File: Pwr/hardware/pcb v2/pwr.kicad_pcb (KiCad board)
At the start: 4 copper layers, 82.8 x 110 mm, 59 parts, among them J1 XT60, J10 Conn_ARM_JTAG_SWD_10, J11 Conn_01x06, J12 Conn_01x06, J13 Conn_01x06, J14 Conn_01x06, J15 XT60, J2 FFC2B35-10-T, J3 114020164, J4 XT60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

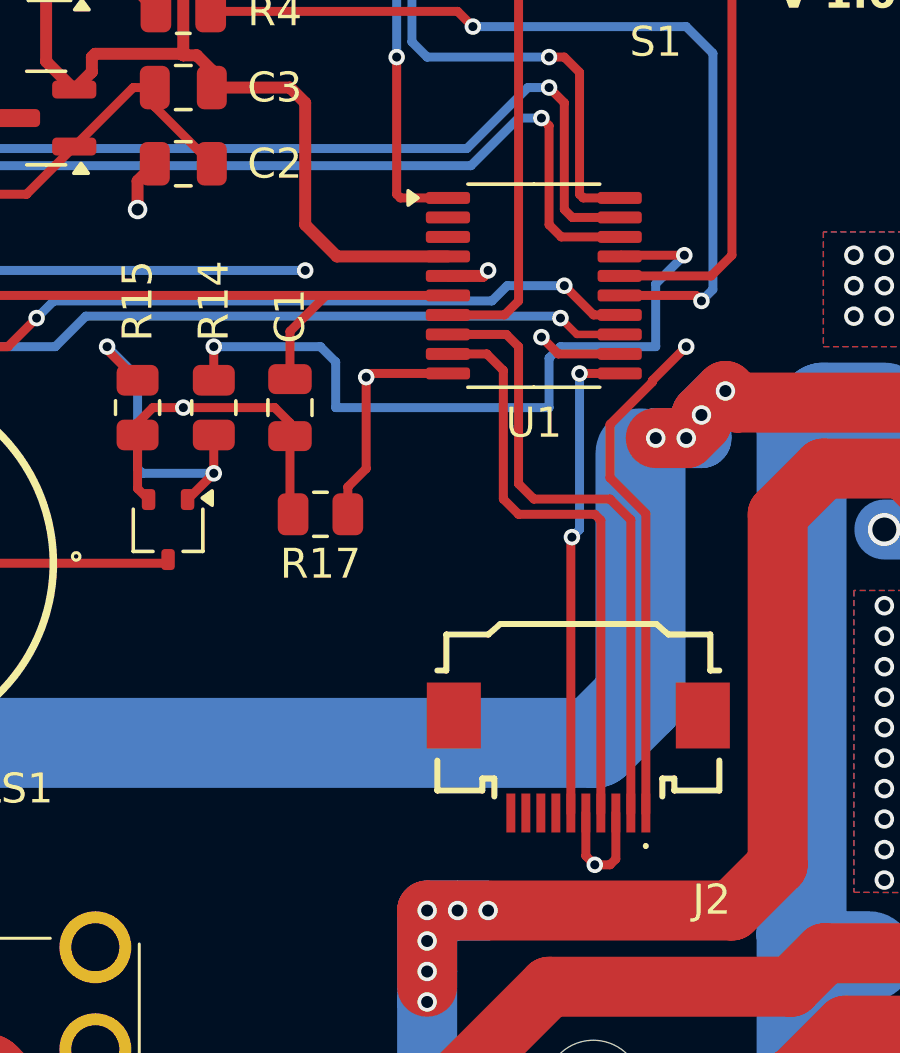
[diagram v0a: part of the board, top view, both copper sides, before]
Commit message: Correction sur l'ecran SPI
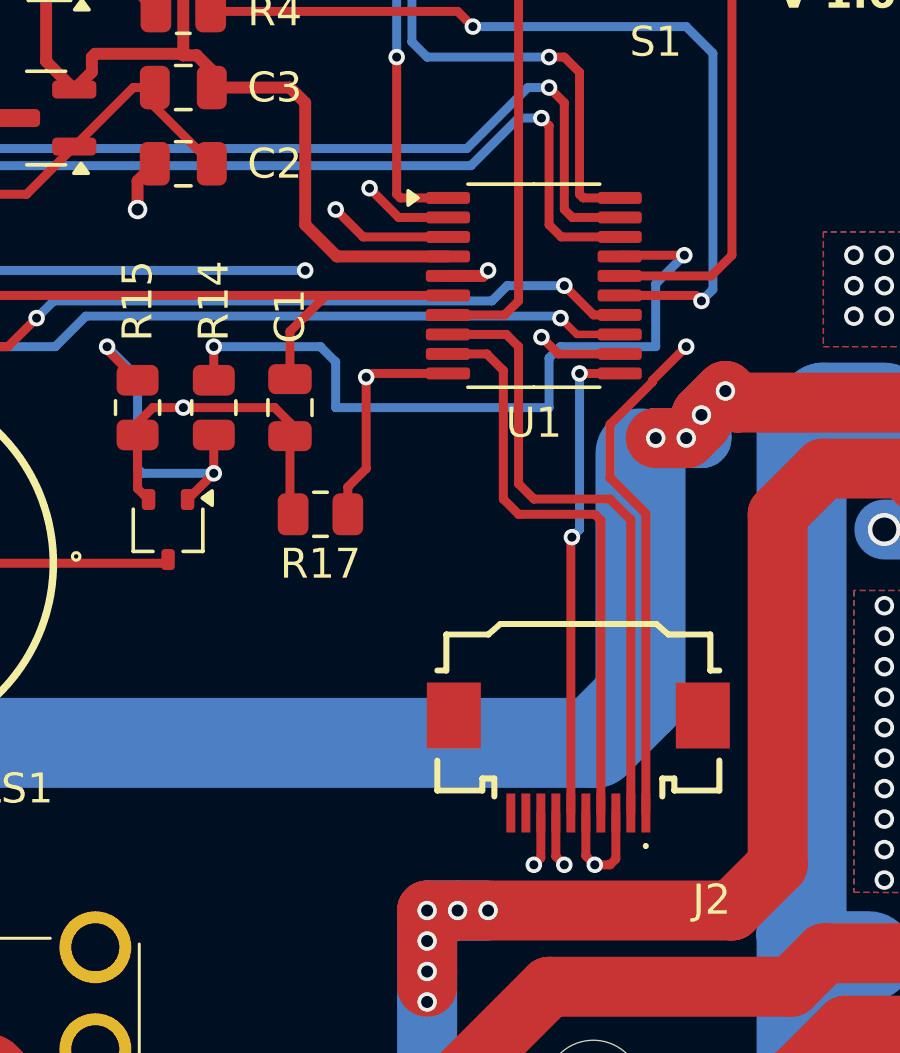
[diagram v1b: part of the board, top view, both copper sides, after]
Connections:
- J2 pad 7: unconnected-(J2-Pad7) -> /CPU - Debug/DISPLAY_RESET
- J2 pad 8: unconnected-(J2-Pad8) -> /CPU - Debug/DISPLAY_CD
- U1 pad 2: unconnected-(U1-PC14-Pad2) -> /CPU - Debug/DISPLAY_CD
- U1 pad 3: unconnected-(U1-PC15-Pad3) -> /CPU - Debug/DISPLAY_RESET
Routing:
- net /CPU - Debug/DISPLAY_CD: track 0.00 -> 41.1 mm, vias 0 -> 2
- net /CPU - Debug/DISPLAY_RESET: track 0.00 -> 37.6 mm, vias 0 -> 2
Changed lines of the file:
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@@
 	(net 56 "unconnected-(RV2-Pad1)")
 	(net 57 "unconnected-(RV3-Pad3)")
-	(net 58 "unconnected-(J2-Pad8)")
+	(net 58 "/CPU - Debug/DISPLAY_CD")
 	(net 59 "Net-(Q4-D)")
 	(net 60 "Net-(Q4-G)")
@@
 	(net 65 "Net-(Q6-G)")
 	(net 66 "/CPU - Debug/BUZZER")
-	(net 67 "unconnected-(U1-PC14-Pad2)")
-	(net 68 "unconnected-(U1-PC15-Pad3)")
-	(net 69 "unconnected-(J2-Pad7)")
-	(net 70 "Net-(R5-Pad2)")
-	(net 71 "Net-(J10-GNDDetect)")
+	(net 67 "/CPU - Debug/DISPLAY_RESET")
+	(net 68 "Net-(R5-Pad2)")
+	(net 69 "Net-(J10-GNDDetect)")
 	(footprint "Capacitor_SMD:C_0805_2012Metric"
 		(layer "F.Cu")
@@
 			(layers "F.Cu" "F.Paste" "F.Mask")
 			(roundrect_rratio 0.25)
-			(net 67 "unconnected-(U1-PC14-Pad2)")
+			(net 58 "/CPU - Debug/DISPLAY_CD")
 			(pinfunction "PC14")
-			(pintype "bidirectional+no_connect")
+			(pintype "bidirectional")
 		)
 		(pad "3" smd roundrect
@@
 			(layers "F.Cu" "F.Paste" "F.Mask")
 			(roundrect_rratio 0.25)
-			(net 68 "unconnected-(U1-PC15-Pad3)")
+			(net 67 "/CPU - Debug/DISPLAY_RESET")
 			(pinfunction "PC15")
-			(pintype "bidirectional+no_connect")
+			(pintype "bidirectional")
 		)
 		(pad "4" smd roundrect
@@
 			(size 0.74 2.79)
 			(layers "F.Cu" "F.Paste" "F.Mask")
-			(net 71 "Net-(J10-GNDDetect)")
+			(net 69 "Net-(J10-GNDDetect)")
 			(pinfunction "GNDDetect")
 			(pintype "passive")
@@
 			)
 			(remove_unused_layers no)
-			(net 70 "Net-(R5-Pad2)")
+			(net 68 "Net-(R5-Pad2)")
 			(pinfunction "6")
 			(pintype "passive")
@@
 			(layers "F.Cu" "F.Paste" "F.Mask")
 			(roundrect_rratio 0.243902)
-			(net 71 "Net-(J10-GNDDetect)")
+			(net 69 "Net-(J10-GNDDetect)")
 			(pintype "passive")
 		)
@@
 			(size 0.3 1.3)
 			(layers "F.Cu" "F.Paste" "F.Mask")
-			(net 69 "unconnected-(J2-Pad7)")
+			(net 67 "/CPU - Debug/DISPLAY_RESET")
 			(pinfunction "7")
-			(pintype "passive+no_connect")
+			(pintype "passive")
 		)
 		(pad "8" smd rect
@@
 			(size 0.3 1.3)
 			(layers "F.Cu" "F.Paste" "F.Mask")
-			(net 58 "unconnected-(J2-Pad8)")
+			(net 58 "/CPU - Debug/DISPLAY_CD")
 			(pinfunction "8")
-			(pintype "passive+no_connect")
+			(pintype "passive")
 		)
 		(pad "9" smd rect
@@
 			(layers "F.Cu" "F.Paste" "F.Mask")
 			(roundrect_rratio 0.243902)
-			(net 70 "Net-(R5-Pad2)")
+			(net 68 "Net-(R5-Pad2)")
 			(pintype "passive")
 		)
@@
 	)
 	(segment
+		(start 160.1 62.503106)
+		(end 160.1 62.5)
+		(width 0.3)
+		(layer "F.Cu")
+		(net 58)
+	)
+	(segment
+		(start 165.81 84.818)
+		(end 165.81 83.325)
+		(width 0.3)
+		(layer "F.Cu")
+		(net 58)
+	)
+	(segment
+		(start 162.7135 63.473)
+		(end 161.069894 63.473)
+		(width 0.3)
+		(layer "F.Cu")
+		(net 58)
+	)
+	(segment
+		(start 161.069894 63.473)
+		(end 160.1 62.503106)
+		(width 0.3)
+		(layer "F.Cu")
+		(net 58)
+	)
+	(segment
+		(start 165.576 85.052)
+		(end 165.81 84.818)
+		(width 0.3)
+		(layer "F.Cu")
+		(net 58)
+	)
+	(via
+		(at 160.1 62.5)
+		(size 0.55)
+		(drill 0.3)
+		(layers "F.Cu" "B.Cu")
+		(net 58)
+	)
+	(via
+		(at 165.576 85.052)
+		(size 0.55)
+		(drill 0.3)
+		(layers "F.Cu" "B.Cu")
+		(net 58)
+	)
+	(segment
+		(start 168.965 69.135)
+		(end 168.624 69.476)
+		(width 0.3)
+		(layer "In1.Cu")
+		(net 58)
+	)
+	(segment
+		(start 168.6 62.5)
+		(end 169.1 63)
+		(width 0.3)
+		(layer "In1.Cu")
+		(net 58)
+	)
+	(segment
+		(start 160.1 62.5)
+		(end 168.6 62.5)
+		(width 0.3)
+		(layer "In1.Cu")
+		(net 58)
+	)
+	(segment
+		(start 168.624 69.476)
+		(end 168.624 86.068)
+		(width 0.3)
+		(layer "In1.Cu")
+		(net 58)
+	)
+	(segment
+		(start 165.576 85.56)
+		(end 165.576 85.052)
+		(width 0.3)
+		(layer "In1.Cu")
+		(net 58)
+	)
+	(segment
+		(start 168.965 63.135)
+		(end 168.965 69.135)
+		(width 0.3)
+		(layer "In1.Cu")
+		(net 58)
+	)
+	(segment
+		(start 169.1 63)
+		(end 168.965 63.135)
+		(width 0.3)
+		(layer "In1.Cu")
+		(net 58)
+	)
+	(segment
+		(start 168.624 86.068)
+		(end 166.084 86.068)
+		(width 0.3)
+		(layer "In1.Cu")
+		(net 58)
+	)
+	(segment
+		(start 166.084 86.068)
+		(end 165.576 85.56)
+		(width 0.3)
+		(layer "In1.Cu")
+		(net 58)
+	)
+	(segment
 		(start 128.492 73.368)
 		(end 129 72.86)
@@
 	)
 	(segment
+		(start 166.592 85.052)
+		(end 166.31 84.77)
+		(width 0.3)
+		(layer "F.Cu")
+		(net 67)
+	)
+	(segment
+		(start 162.7135 64.123)
+		(end 159.887 64.123)
+		(width 0.3)
+		(layer "F.Cu")
+		(net 67)
+	)
+	(segment
+		(start 166.31 84.77)
+		(end 166.31 83.325)
+		(width 0.3)
+		(layer "F.Cu")
+		(net 67)
+	)
+	(segment
+		(start 159.887 64.123)
+		(end 158.972 63.208)
+		(width 0.3)
+		(layer "F.Cu")
+		(net 67)
+	)
+	(via
+		(at 158.972 63.208)
+		(size 0.55)
+		(drill 0.3)
+		(layers "F.Cu" "B.Cu")
+		(net 67)
+	)
+	(via
+		(at 166.592 85.052)
+		(size 0.55)
+		(drill 0.3)
+		(layers "F.Cu" "B.Cu")
+		(net 67)
+	)
+	(segment
+		(start 168.116 63.208)
+		(end 168.116 83.528)
+		(width 0.3)
+		(layer "In1.Cu")
+		(net 67)
+	)
+	(segment
+		(start 158.972 63.208)
+		(end 168.116 63.208)
+		(width 0.3)
+		(layer "In1.Cu")
+		(net 67)
+	)
+	(segment
+		(start 168.116 83.528)
+		(end 166.592 85.052)
+		(width 0.3)
+		(layer "In1.Cu")
+		(net 67)
+	)
+	(segment
 		(start 163.253 52.032)
 		(end 163.335 51.95)
 		(width 0.4)
 		(layer "F.Cu")
-		(net 70)
+		(net 68)
 	)
 	(segment
@@
 		(width 0.4)
 		(layer "F.Cu")
-		(net 70)
+		(net 68)
 	)
 	(segment
@@
 		(width 0.3)
 		(layer "F.Cu")
-		(net 71)
+		(net 69)
 	)
 	(segment
@@
 		(width 0.3)
 		(layer "F.Cu")
-		(net 71)
+		(net 69)
 	)
 	(segment
@@
 		(width 0.3)
 		(layer "F.Cu")
-		(net 71)
+		(net 69)
 	)
 	(zone
